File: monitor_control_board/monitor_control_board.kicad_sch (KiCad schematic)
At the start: 10 parts, among them J1 Conn_01x08_Male, J2 Conn_01x08_Male, J3 Conn_01x08_Male, SW1 SW_Push, SW2 SW_Push, SW3 SW_Push, SW4 SW_Push, SW5 SW_Push, SW6 SW_Push

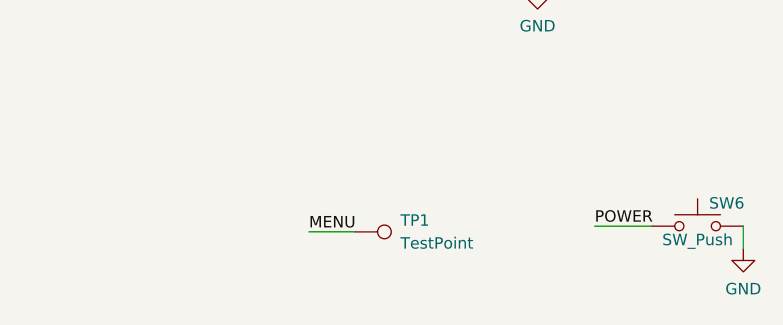
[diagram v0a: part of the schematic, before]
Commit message: monitor control board에 GND TP 추가
Signed-off-by: Ju, Gyeong-min <jcmh74@gmail.com>
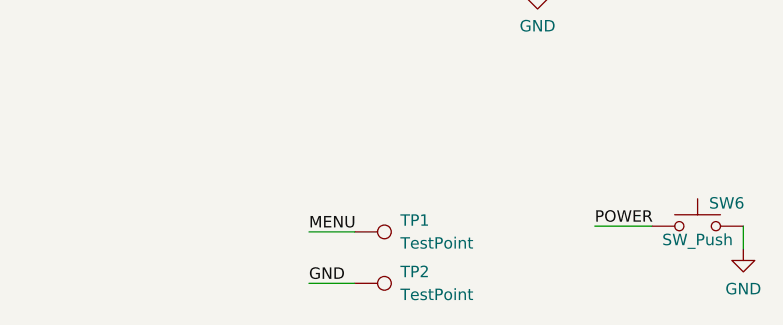
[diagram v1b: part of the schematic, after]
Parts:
- added TP2: TestPoint, TestPoint:TestPoint_Pad_D2.0mm, symbol Connector:TestPoint
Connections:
- net GND: now also TP2.1
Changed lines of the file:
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@@
+    (stroke (width 0) (type default) (color 0 0 0 0))
+  )
+  (wire (pts (xy 188.595 133.35) (xy 193.675 133.35))
     (stroke (width 0) (type default) (color 0 0 0 0))
   )
@@
   (label "DOWN" (at 71.12 98.425 180)
     (effects (font (size 1.27 1.27)) (justify right bottom))
+  )
+  (label "GND" (at 188.595 133.35 0)
+    (effects (font (size 1.27 1.27)) (justify left bottom))
   )
   (label "MENU" (at 71.12 106.045 180)
@@
     (pin "8")
   )
+  (symbol (lib_id "Connector:TestPoint") (at 193.675 133.35 270) (unit 1)
+    (in_bom yes) (on_board yes) (fields_autoplaced)
+    (property "Reference" "TP2" (id 0) (at 198.755 132.0799 90)
+      (effects (font (size 1.27 1.27)) (justify left))
+    )
+    (property "Value" "TestPoint" (id 1) (at 198.755 134.6199 90)
+      (effects (font (size 1.27 1.27)) (justify left))
+    )
+    (property "Footprint" "TestPoint:TestPoint_Pad_D2.0mm" (id 2) (at 193.675 138.43 0)
+      (effects (font (size 1.27 1.27)) hide)
+    )
+    (property "Datasheet" "~" (id 3) (at 193.675 138.43 0)
+      (effects (font (size 1.27 1.27)) hide)
+    )
+    (pin "1")
+  )
   (symbol (lib_id "Switch:SW_Push") (at 186.055 74.93 0) (unit 1)
     (in_bom yes) (on_board yes) (fields_autoplaced)
@@
       (reference "TP1") (unit 1) (value "TestPoint") (footprint "TestPoint:TestPoint_Pad_D2.0mm")
     )
-  )
+    (path "/c9f71dc3-2b4a-4ca2-8db0-36825f55689f"
+      (reference "TP2") (unit 1) (value "TestPoint") (footprint "TestPoint:TestPoint_Pad_D2.0mm")
+    )
+  )

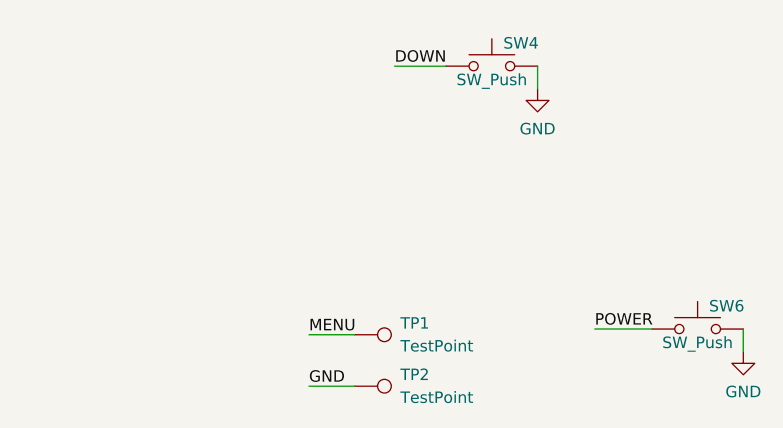
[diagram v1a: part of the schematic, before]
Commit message: monitor_control_board rev2 업데이트
Signed-off-by: Ju, Gyeong-min <jcmh74@gmail.com>
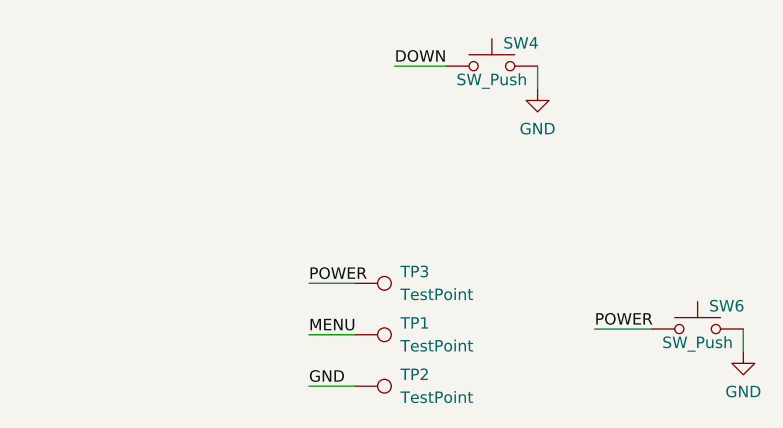
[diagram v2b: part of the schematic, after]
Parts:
- added TP3: TestPoint, TestPoint:TestPoint_THTPad_D2.0mm_Drill1.0mm, symbol Connector:TestPoint
- TP1, TP2: footprint TestPoint:TestPoint_Pad_D2.0mm -> TestPoint:TestPoint_THTPad_D2.0mm_Drill1.0mm
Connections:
- net POWER: now also TP3.1
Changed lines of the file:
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@@
+    (stroke (width 0) (type default) (color 0 0 0 0))
+  )
+  (wire (pts (xy 188.595 121.92) (xy 193.675 121.92))
     (stroke (width 0) (type default) (color 0 0 0 0))
   )
@@
   (label "DOWN" (at 71.12 98.425 180)
     (effects (font (size 1.27 1.27)) (justify right bottom))
+  )
+  (label "POWER" (at 188.595 121.92 0)
+    (effects (font (size 1.27 1.27)) (justify left bottom))
   )
   (label "GND" (at 188.595 133.35 0)
@@
     (pin "2")
   )
+  (symbol (lib_id "Connector:TestPoint") (at 193.675 121.92 270) (unit 1)
+    (in_bom yes) (on_board yes) (fields_autoplaced)
+    (property "Reference" "TP3" (id 0) (at 198.755 120.6499 90)
+      (effects (font (size 1.27 1.27)) (justify left))
+    )
+    (property "Value" "TestPoint" (id 1) (at 198.755 123.1899 90)
+      (effects (font (size 1.27 1.27)) (justify left))
+    )
+    (property "Footprint" "TestPoint:TestPoint_THTPad_D2.0mm_Drill1.0mm" (id 2) (at 193.675 127 0)
+      (effects (font (size 1.27 1.27)) hide)
+    )
+    (property "Datasheet" "~" (id 3) (at 193.675 127 0)
+      (effects (font (size 1.27 1.27)) hide)
+    )
+    (pin "1")
+  )
   (symbol (lib_id "power:GND") (at 213.995 76.835 0) (unit 1)
     (in_bom yes) (on_board yes)
@@
       (effects (font (size 1.27 1.27)) (justify left))
     )
-    (property "Footprint" "TestPoint:TestPoint_Pad_D2.0mm" (id 2) (at 193.675 132.715 0)
+    (property "Footprint" "TestPoint:TestPoint_THTPad_D2.0mm_Drill1.0mm" (id 2) (at 193.675 132.715 0)
       (effects (font (size 1.27 1.27)) hide)
     )
@@
       (effects (font (size 1.27 1.27)) (justify left))
     )
-    (property "Footprint" "TestPoint:TestPoint_Pad_D2.0mm" (id 2) (at 193.675 138.43 0)
+    (property "Footprint" "TestPoint:TestPoint_THTPad_D2.0mm_Drill1.0mm" (id 2) (at 193.675 138.43 0)
       (effects (font (size 1.27 1.27)) hide)
     )
@@
     )
     (path "/3b934f31-2bae-48a3-8048-7da2c4d085a5"
-      (reference "TP1") (unit 1) (value "TestPoint") (footprint "TestPoint:TestPoint_Pad_D2.0mm")
+      (reference "TP1") (unit 1) (value "TestPoint") (footprint "TestPoint:TestPoint_THTPad_D2.0mm_Drill1.0mm")
     )
     (path "/c9f71dc3-2b4a-4ca2-8db0-36825f55689f"
-      (reference "TP2") (unit 1) (value "TestPoint") (footprint "TestPoint:TestPoint_Pad_D2.0mm")
-    )
-  )
+      (reference "TP2") (unit 1) (value "TestPoint") (footprint "TestPoint:TestPoint_THTPad_D2.0mm_Drill1.0mm")
+    )
+    (path "/28135604-dc7c-4d8f-bee5-8abb6d80f68a"
+      (reference "TP3") (unit 1) (value "TestPoint") (footprint "TestPoint:TestPoint_THTPad_D2.0mm_Drill1.0mm")
+    )
+  )

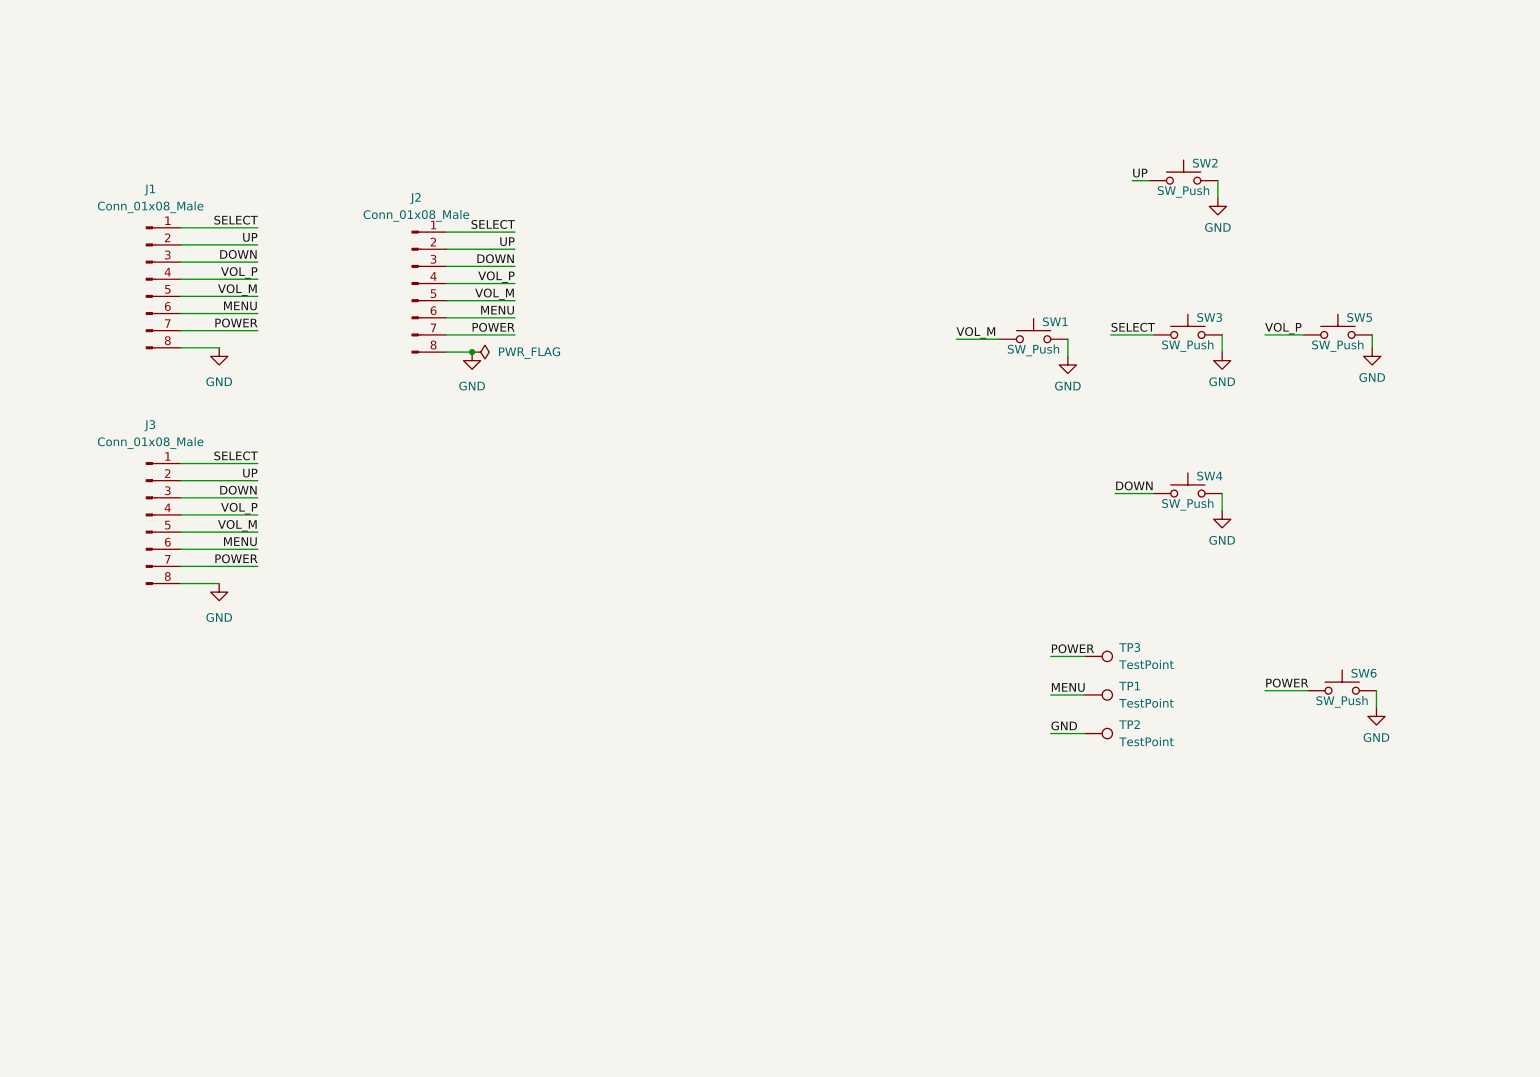
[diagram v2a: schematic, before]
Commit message: rasp_power_module smt 관련 작업 추가 및 monitor_control_board 개선
Signed-off-by: Ju, Gyeong-min <jcmh74@gmail.com>
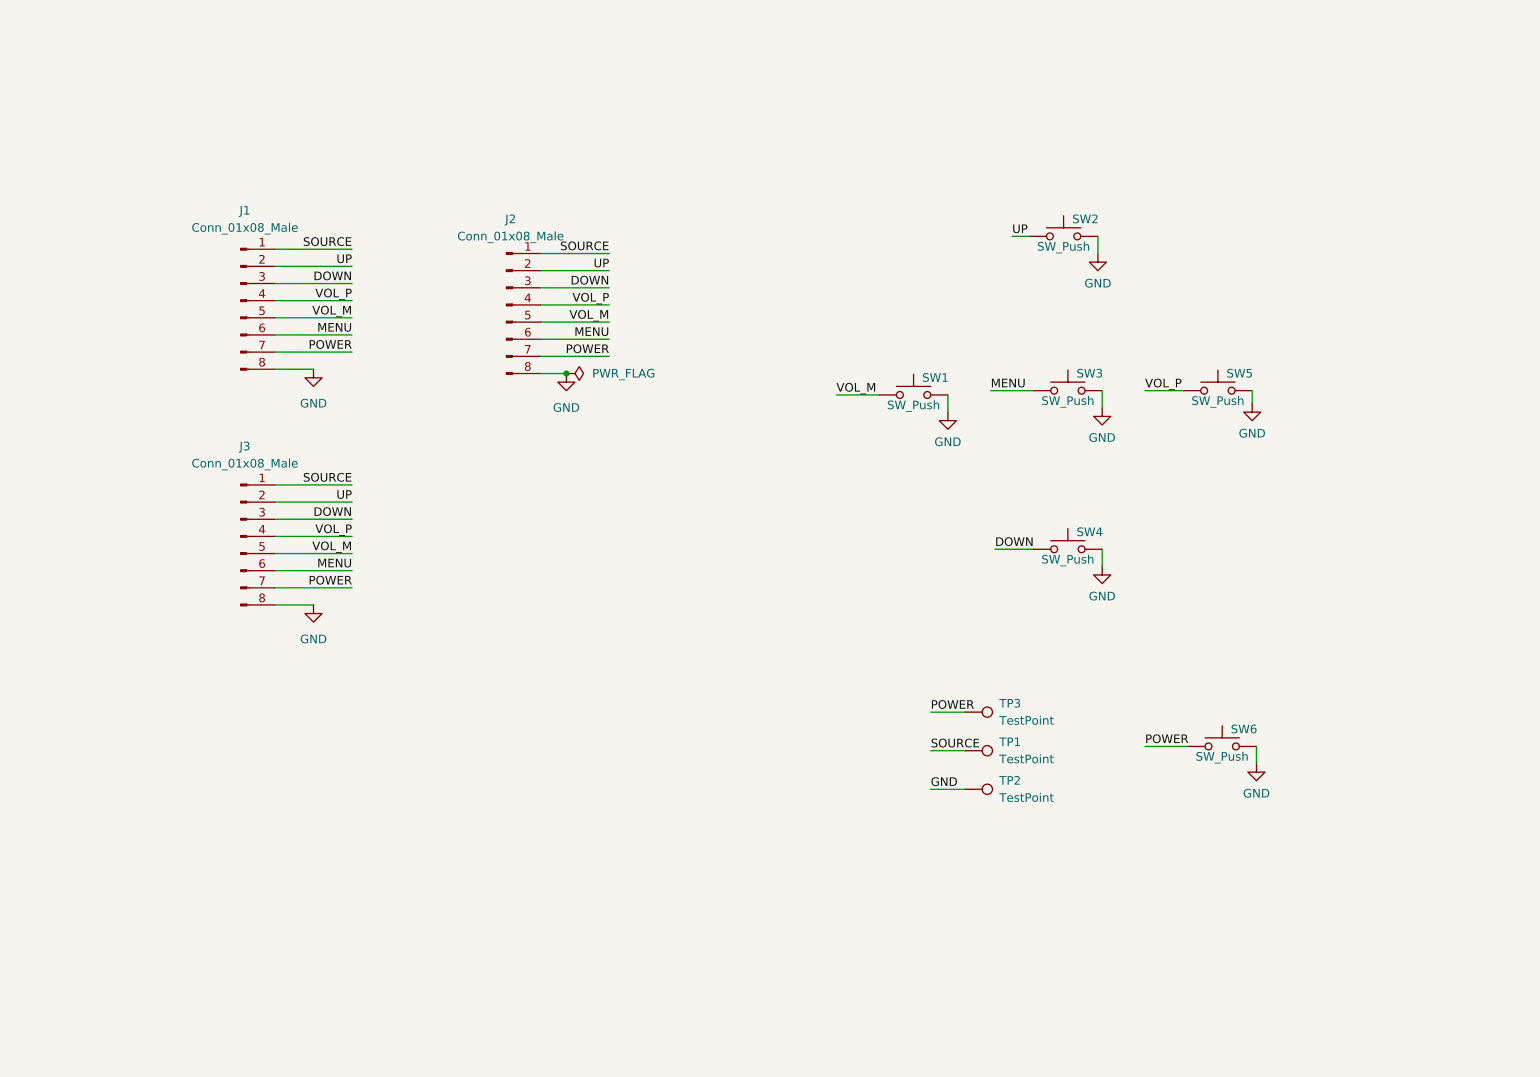
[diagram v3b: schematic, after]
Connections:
- net MENU: now also SW3.1; no longer TP1.1
- net SELECT renamed SOURCE
- net SOURCE: now also TP1.1; no longer SW3.1
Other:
- moved on the sheet: J1, J2, J3, SW1, SW2, SW3, SW4, SW5, SW6, TP1, TP2, TP3

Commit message: OSD 컨트롤 보드에 IR수신 파트 추가
Signed-off-by: Ju, Gyeong-min <jcmh74@gmail.com>
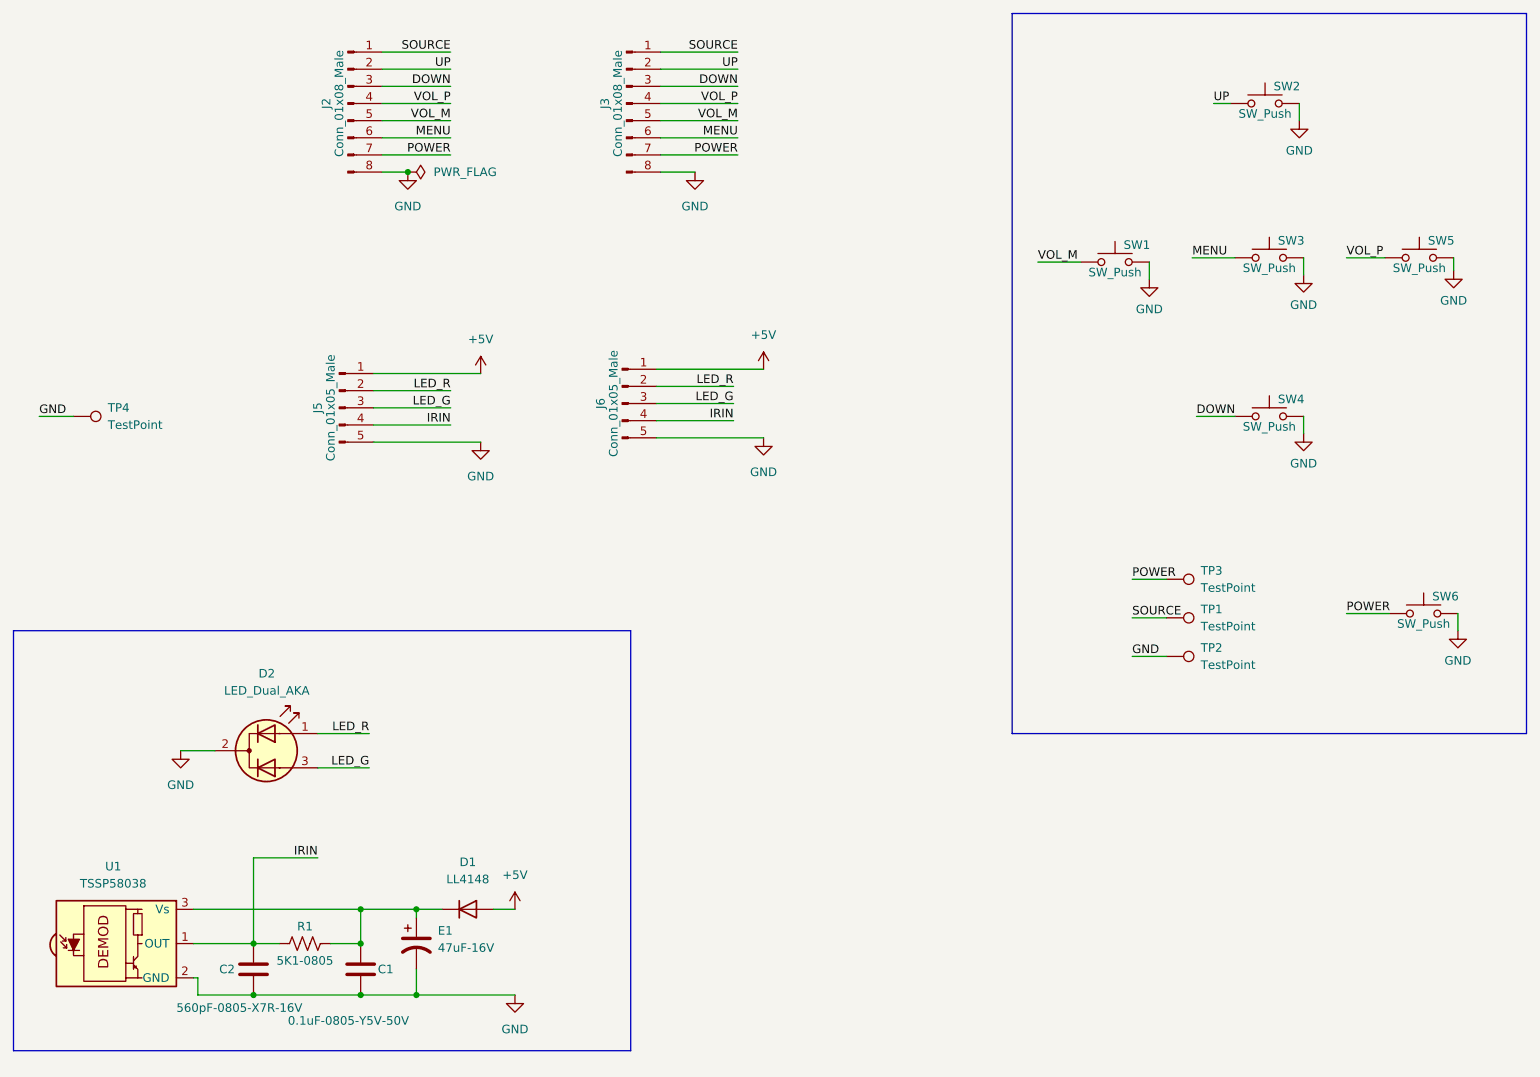
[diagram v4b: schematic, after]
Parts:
- removed J1: Conn_01x08_Male, Connector_JST:JST_GH_SM08B-GHS-TB_1x08-1MP_P1.25mm_Horizontal, symbol Connector:Conn_01x08_Male
- added C1: 0.1uF-0805-Y5V-50V, Capacitor_SMD:C_0805_2012Metric_Pad1.18x1.45mm_HandSolder, symbol Device:C
- added C2: 560pF-0805-X7R-16V, Capacitor_SMD:C_0805_2012Metric_Pad1.18x1.45mm_HandSolder, symbol Device:C
- added D1: LL4148, Diode_SMD:D_MiniMELF, symbol Diode:LL4148
- added D2: LED_Dual_AKA, LED_THT:LED_D3.0mm-3, symbol Device:LED_Dual_AKA
- added E1: 47uF-16V, Capacitor_SMD:CP_Elec_4x5.4, symbol Device:C_Polarized_US
- added J5: Conn_01x05_Male, Connector_PinHeader_2.54mm:PinHeader_1x05_P2.54mm_Vertical, symbol Connector:Conn_01x05_Male
- added J6: Conn_01x05_Male, Connector_JST:JST_PH_S5B-PH-K_1x05_P2.00mm_Horizontal, symbol Connector:Conn_01x05_Male
- added R1: 5K1-0805, Resistor_SMD:R_0805_2012Metric_Pad1.20x1.40mm_HandSolder, symbol Device:R_US
- added TP4: TestPoint, TestPoint:TestPoint_THTPad_D2.0mm_Drill1.0mm, symbol Connector:TestPoint
- added U1: TSSP58038, OptoDevice:Vishay_MINICAST-3Pin, symbol Sensor_Proximity:TSSP58038SS1XB
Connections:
- net GND: now also C1.2, C2.2, D2.2 (K), E1.2, J5.5 (Pin_5), J6.5 (Pin_5), TP4.1, U1.2 (GND)
- new net: C1.1, D1.1 (K), E1.1, R1.2, U1.3 (Vs)
- new net +5V: D1.2 (A), J5.1 (Pin_1), J6.1 (Pin_1)
- new net IRIN: C2.1, J5.4 (Pin_4), J6.4 (Pin_4), R1.1, U1.1 (OUT)
- new net LED_G: D2.3 (A2), J5.3 (Pin_3), J6.3 (Pin_3)
- new net LED_R: D2.1 (A1), J5.2 (Pin_2), J6.2 (Pin_2)
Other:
- moved on the sheet: J2, J3, SW1, SW2, SW3, SW4, SW5, SW6, TP1, TP2, TP3

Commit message: PCB 배선 최적화
Signed-off-by: Ju, Gyeong-min <jcmh74@gmail.com>
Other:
- moved on the sheet: C1, C2, D1, D2, E1, J2, J3, J5, J6, R1, SW1, SW2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
